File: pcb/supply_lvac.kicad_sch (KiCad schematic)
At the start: 46 parts

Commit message: Start layout
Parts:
- added H1, H2, H3, H4: MountingHole, MountingHole:MountingHole_3.2mm_M3, symbol Mechanical:MountingHole
- C1, C2, C3, C4, C5, C6: renamed from C?; footprint (none) -> Capacitor_THT:CP_Radial_D16.0mm_P7.50mm
- C10: renamed from C?; footprint (none) -> Capacitor_THT:CP_Radial_D4.0mm_P1.50mm
- C11, C12, C13, C14, C15, C16, C17, C18, C19, C20, C21, C22, C23, C24, C25, C26, C8: renamed from C?; footprint (none) -> Capacitor_THT:CP_Radial_D4.0mm_P2.00mm
- C7, C9: renamed from C?; footprint (none) -> Capacitor_THT:C_Disc_D3.0mm_W1.6mm_P2.50mm
- D6, D7: renamed from D?; footprint (none) -> LED_THT:LED_D5.0mm
- J1: renamed from J?; footprint (none) -> Connector_Molex:Molex_KK-254_AE-6410-02A_1x02_P2.54mm_Vertical
- J2, J3, J4, J5, J6, J7, J8, J9: renamed from J?; footprint (none) -> Connector_IDC:IDC-Header_2x05_P2.54mm_Vertical
- R1, R2: renamed from R?; footprint (none) -> Resistor_THT:R_Axial_DIN0207_L6.3mm_D2.5mm_P10.16mm_Horizontal
- U1, U2: renamed from U?; footprint (none) -> Package_TO_SOT_THT:TO-220-3_Vertical
- gave numbers to parts that had none: 5
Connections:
- net GND: now also C2.2, C5.1; no longer C2.1, C5.2
- net VREC+: now also C2.1; no longer C5.1
- net VREC-: now also C5.2; no longer C2.2
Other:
- moved on the sheet: C1, C10, C11, C12, C13, C14, C15, C16, C17, C18, C19, C2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

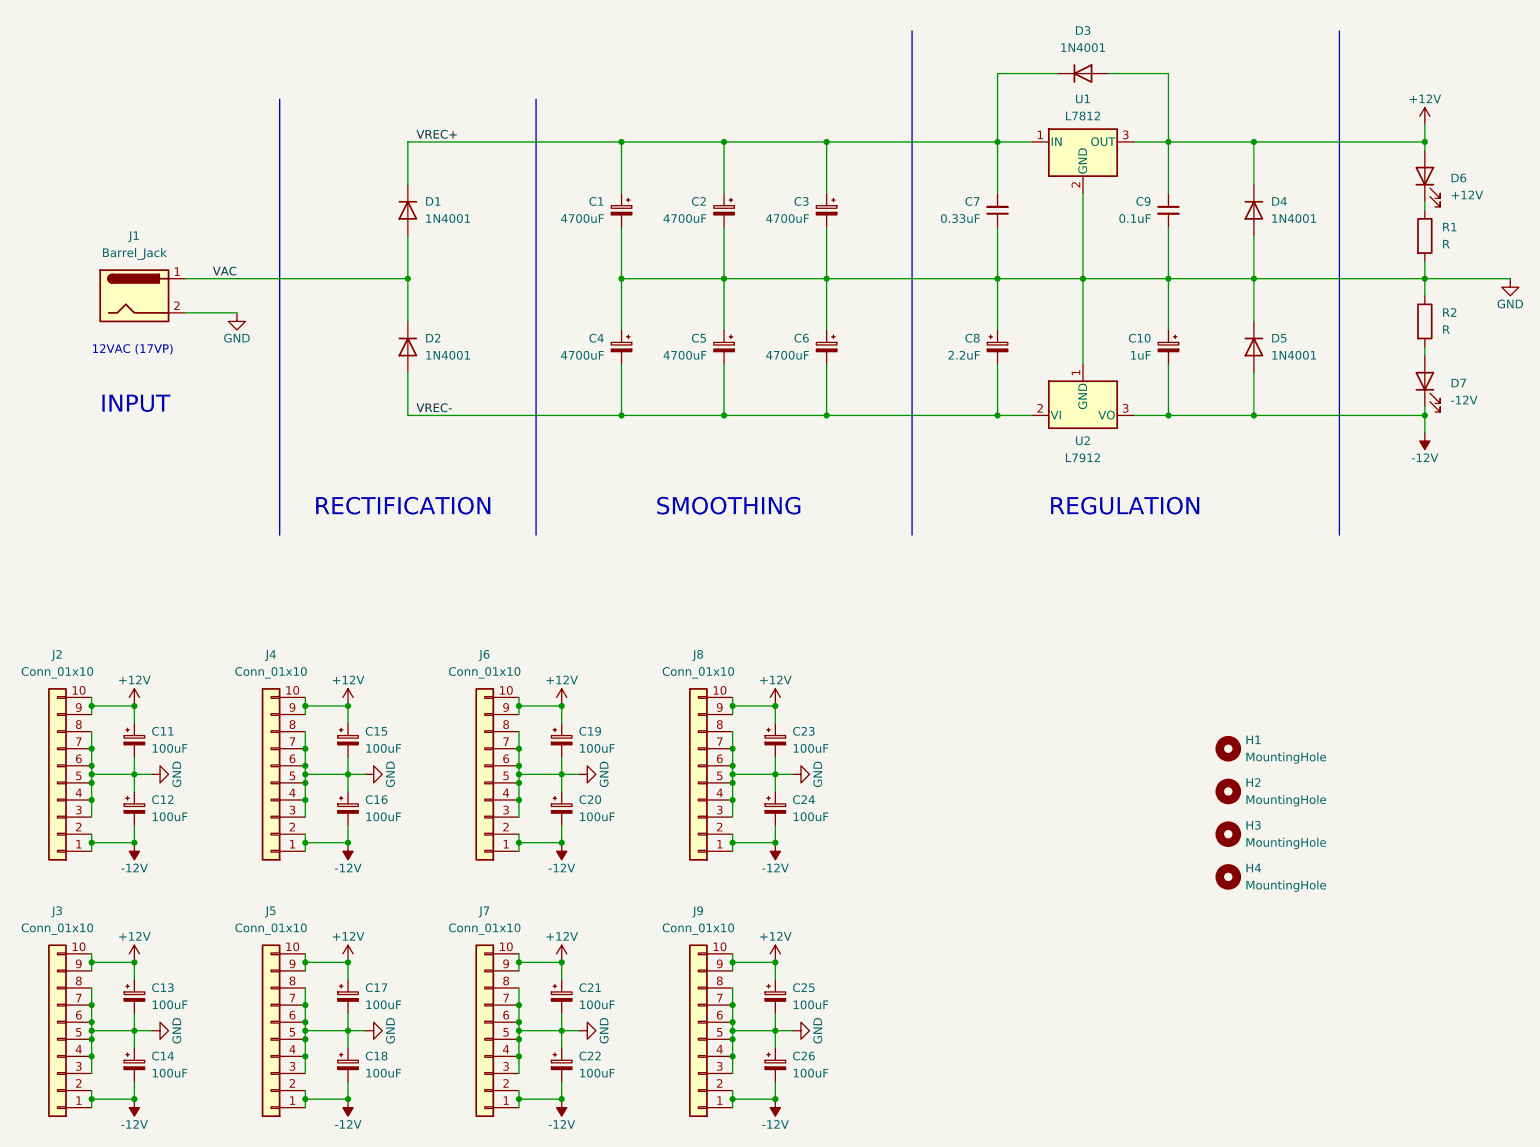
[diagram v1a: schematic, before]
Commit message: Start via stitching
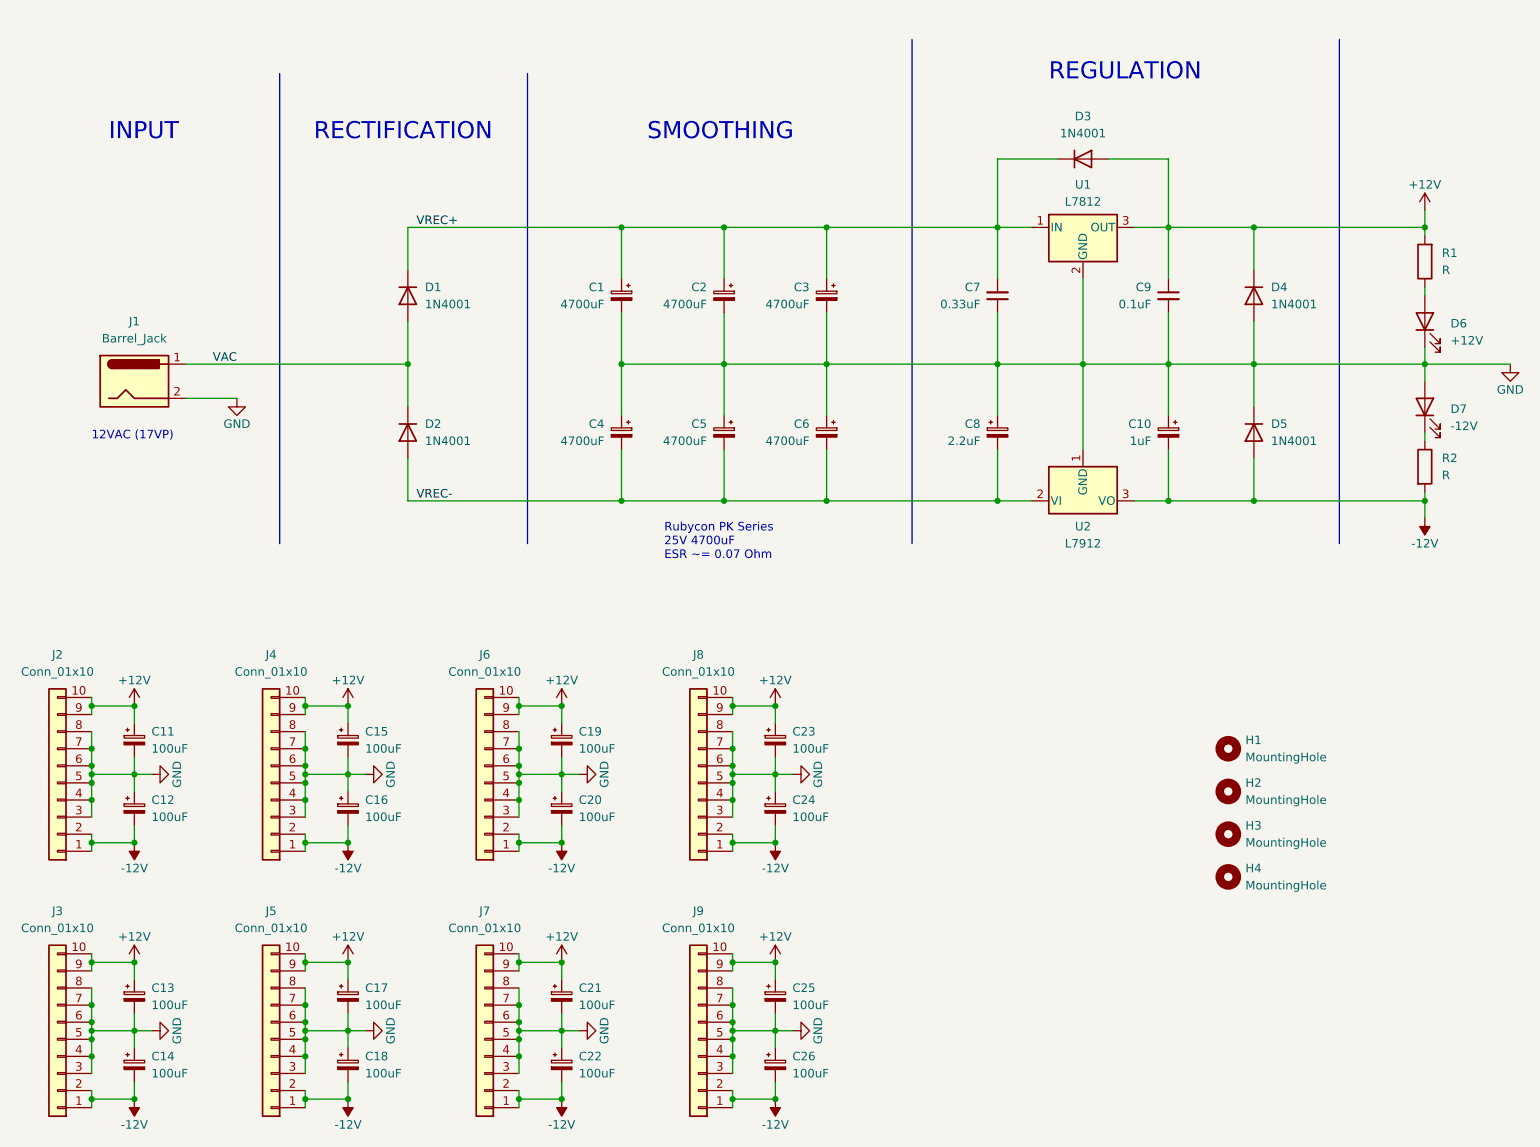
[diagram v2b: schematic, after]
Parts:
- R1, R2: footprint Resistor_THT:R_Axial_DIN0207_L6.3mm_D2.5mm_P10.16mm_Horizontal -> Resistor_THT:R_Axial_DIN0207_L6.3mm_D2.5mm_P2.54mm_Vertical
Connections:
- net +12V: now also R1.2; no longer D6.2 (A)
- net -12V: now also R2.2; no longer D7.1 (K)
- net GND: now also D6.1 (K), D7.2 (A); no longer R1.2, R2.1
- net at R1.1: now also D6.2 (A); no longer D6.1 (K)
- new net: D7.1 (K), R2.1
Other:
- note added: "Rubycon PK Series 25V 4700uF ESR ~= 0.07 Ohm"
- moved on the sheet: C1, C10, C2, C3, C4, C5, C6, C7, C8, C9, D1, D2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

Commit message: Complete layout. Export gerbers
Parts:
- removed C25, C26: 100uF, Capacitor_THT:CP_Radial_D4.0mm_P2.00mm, symbol Device:C_Polarized_Small
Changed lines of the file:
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@@
   (junction (at 132.08 125.73) (diameter 0) (color 0 0 0 0)
   )
-  (junction (at 138.43 173.99) (diameter 0) (color 0 0 0 0)
-  )
   (junction (at 43.18 173.99) (diameter 0) (color 0 0 0 0)
   )
@@
   (junction (at 209.55 74.93) (diameter 0) (color 0 0 0 0)
   )
-  (junction (at 138.43 184.15) (diameter 0) (color 0 0 0 0)
-  )
   (junction (at 74.93 163.83) (diameter 0) (color 0 0 0 0)
   )
-  (junction (at 138.43 163.83) (diameter 0) (color 0 0 0 0)
-  )
   (junction (at 43.18 135.89) (diameter 0) (color 0 0 0 0)
   )
@@
     (stroke (width 0) (type default) (color 0 0 0 0))
   )
-  (wire (pts (xy 138.43 181.61) (xy 138.43 184.15))
-    (stroke (width 0) (type default) (color 0 0 0 0))
-  )
   (wire (pts (xy 74.93 181.61) (xy 74.93 184.15))
     (stroke (width 0) (type default) (color 0 0 0 0))
@@
     (stroke (width 0) (type default) (color 0 0 0 0))
   )
+  (wire (pts (xy 68.58 172.72) (xy 68.58 173.99))
+    (stroke (width 0) (type default) (color 0 0 0 0))
+  )
+  (polyline (pts (xy 158.75 26.67) (xy 158.75 101.6))
+    (stroke (width 0) (type default) (color 0 0 0 0))
+  )
+  (wire (pts (xy 36.83 163.83) (xy 36.83 165.1))
+    (stroke (width 0) (type default) (color 0 0 0 0))
+  )
+  (wire (pts (xy 100.33 162.56) (xy 100.33 163.83))
+    (stroke (width 0) (type default) (color 0 0 0 0))
+  )
+  (wire (pts (xy 83.82 88.9) (xy 83.82 95.25))
+    (stroke (width 0) (type default) (color 0 0 0 0))
+  )
+  (wire (pts (xy 74.93 143.51) (xy 74.93 146.05))
+    (stroke (width 0) (type default) (color 0 0 0 0))
+  )
+  (wire (pts (xy 209.55 68.58) (xy 209.55 74.93))
+    (stroke (width 0) (type default) (color 0 0 0 0))
+  )
+  (wire (pts (xy 36.83 184.15) (xy 36.83 185.42))
+    (stroke (width 0) (type default) (color 0 0 0 0))
+  )
+  (wire (pts (xy 138.43 135.89) (xy 138.43 138.43))
+    (stroke (width 0) (type default) (color 0 0 0 0))
+  )
+  (wire (pts (xy 100.33 139.7) (xy 100.33 142.24))
+    (stroke (width 0) (type default) (color 0 0 0 0))
+  )
+  (wire (pts (xy 36.83 124.46) (xy 36.83 125.73))
+    (stroke (width 0) (type default) (color 0 0 0 0))
+  )
+  (wire (pts (xy 68.58 177.8) (xy 68.58 180.34))
+    (stroke (width 0) (type default) (color 0 0 0 0))
+  )
+  (wire (pts (xy 115.57 74.93) (xy 130.81 74.93))
+    (stroke (width 0) (type default) (color 0 0 0 0))
+  )
+  (wire (pts (xy 36.83 175.26) (xy 36.83 177.8))
+    (stroke (width 0) (type default) (color 0 0 0 0))
+  )
+  (wire (pts (xy 106.68 171.45) (xy 106.68 173.99))
+    (stroke (width 0) (type default) (color 0 0 0 0))
+  )
   (wire (pts (xy 132.08 173.99) (xy 138.43 173.99))
     (stroke (width 0) (type default) (color 0 0 0 0))
   )
-  (wire (pts (xy 68.58 172.72) (xy 68.58 173.99))
-    (stroke (width 0) (type default) (color 0 0 0 0))
-  )
-  (polyline (pts (xy 158.75 26.67) (xy 158.75 101.6))
-    (stroke (width 0) (type default) (color 0 0 0 0))
-  )
-  (wire (pts (xy 36.83 163.83) (xy 36.83 165.1))
-    (stroke (width 0) (type default) (color 0 0 0 0))
-  )
-  (wire (pts (xy 100.33 162.56) (xy 100.33 163.83))
-    (stroke (width 0) (type default) (color 0 0 0 0))
-  )
-  (wire (pts (xy 138.43 173.99) (xy 138.43 176.53))
-    (stroke (width 0) (type default) (color 0 0 0 0))
-  )
-  (wire (pts (xy 83.82 88.9) (xy 83.82 95.25))
-    (stroke (width 0) (type default) (color 0 0 0 0))
-  )
-  (wire (pts (xy 74.93 143.51) (xy 74.93 146.05))
-    (stroke (width 0) (type default) (color 0 0 0 0))
-  )
-  (wire (pts (xy 209.55 68.58) (xy 209.55 74.93))
-    (stroke (width 0) (type default) (color 0 0 0 0))
-  )
-  (wire (pts (xy 36.83 184.15) (xy 36.83 185.42))
-    (stroke (width 0) (type default) (color 0 0 0 0))
-  )
-  (wire (pts (xy 138.43 135.89) (xy 138.43 138.43))
-    (stroke (width 0) (type default) (color 0 0 0 0))
-  )
-  (wire (pts (xy 100.33 139.7) (xy 100.33 142.24))
-    (stroke (width 0) (type default) (color 0 0 0 0))
-  )
-  (wire (pts (xy 36.83 124.46) (xy 36.83 125.73))
-    (stroke (width 0) (type default) (color 0 0 0 0))
-  )
-  (wire (pts (xy 68.58 177.8) (xy 68.58 180.34))
-    (stroke (width 0) (type default) (color 0 0 0 0))
-  )
-  (wire (pts (xy 115.57 74.93) (xy 130.81 74.93))
-    (stroke (width 0) (type default) (color 0 0 0 0))
-  )
-  (wire (pts (xy 36.83 175.26) (xy 36.83 177.8))
-    (stroke (width 0) (type default) (color 0 0 0 0))
-  )
-  (wire (pts (xy 106.68 171.45) (xy 106.68 173.99))
-    (stroke (width 0) (type default) (color 0 0 0 0))
-  )
-  (wire (pts (xy 138.43 173.99) (xy 140.97 173.99))
-    (stroke (width 0) (type default) (color 0 0 0 0))
-  )
   (wire (pts (xy 36.83 177.8) (xy 36.83 180.34))
     (stroke (width 0) (type default) (color 0 0 0 0))
@@
     (stroke (width 0) (type default) (color 0 0 0 0))
   )
-  (wire (pts (xy 138.43 171.45) (xy 138.43 173.99))
-    (stroke (width 0) (type default) (color 0 0 0 0))
-  )
   (wire (pts (xy 130.81 82.55) (xy 130.81 74.93))
     (stroke (width 0) (type default) (color 0 0 0 0))
@@
   )
   (wire (pts (xy 43.18 163.83) (xy 43.18 166.37))
-    (stroke (width 0) (type default) (color 0 0 0 0))
-  )
-  (wire (pts (xy 138.43 163.83) (xy 138.43 166.37))
     (stroke (width 0) (type default) (color 0 0 0 0))
   )
@@
     )
   )
-  (symbol (lib_id "power:GND") (at 140.97 173.99 90) (unit 1)
-    (in_bom yes) (on_board yes)
-    (property "Reference" "#PWR028" (id 0) (at 147.32 173.99 0)
-      (effects (font (size 1.27 1.27)) hide)
-    )
-    (property "Value" "GND" (id 1) (at 144.78 173.99 0))
-    (property "Footprint" "" (id 2) (at 140.97 173.99 0)
-      (effects (font (size 1.27 1.27)) hide)
-    )
-    (property "Datasheet" "" (id 3) (at 140.97 173.99 0)
+  (symbol (lib_id "power:GND") (at 138.43 173.99 0) (unit 1)
+    (in_bom yes) (on_board yes)
+    (property "Reference" "#PWR028" (id 0) (at 138.43 180.34 0)
+      (effects (font (size 1.27 1.27)) hide)
+    )
+    (property "Value" "GND" (id 1) (at 138.43 177.8 0))
+    (property "Footprint" "" (id 2) (at 138.43 173.99 0)
+      (effects (font (size 1.27 1.27)) hide)
+    )
+    (property "Datasheet" "" (id 3) (at 138.43 173.99 0)
       (effects (font (size 1.27 1.27)) hide)
     )
@@
     (pin "1")
   )
-  (symbol (lib_id "Device:C_Polarized_Small") (at 138.43 168.91 0) (unit 1)
-    (in_bom yes) (on_board yes)
-    (property "Reference" "C25" (id 0) (at 140.97 167.64 0)
-      (effects (font (size 1.27 1.27)) (justify left))
-    )
-    (property "Value" "100uF" (id 1) (at 140.97 170.18 0)
-      (effects (font (size 1.27 1.27)) (justify left))
-    )
-    (property "Footprint" "Capacitor_THT:CP_Radial_D4.0mm_P2.00mm" (id 2) (at 138.43 168.91 0)
-      (effects (font (size 1.27 1.27)) hide)
-    )
-    (property "Datasheet" "~" (id 3) (at 138.43 168.91 0)
-      (effects (font (size 1.27 1.27)) hide)
-    )
-    (pin "1")
-    (pin "2")
-  )
   (symbol (lib_id "Connector_Generic:Conn_01x10") (at 127 175.26 180) (unit 1)
     (in_bom yes) (on_board yes) (fields_autoplaced)
@@
     (pin "2")
   )
-  (symbol (lib_id "Device:C_Polarized_Small") (at 138.43 179.07 0) (unit 1)
-    (in_bom yes) (on_board yes)
-    (property "Reference" "C26" (id 0) (at 140.97 177.8 0)
-      (effects (font (size 1.27 1.27)) (justify left))
-    )
-    (property "Value" "100uF" (id 1) (at 140.97 180.34 0)
-      (effects (font (size 1.27 1.27)) (justify left))
-    )
-    (property "Footprint" "Capacitor_THT:CP_Radial_D4.0mm_P2.00mm" (id 2) (at 138.43 179.07 0)
-      (effects (font (size 1.27 1.27)) hide)
-    )
-    (property "Datasheet" "~" (id 3) (at 138.43 179.07 0)
-      (effects (font (size 1.27 1.27)) hide)
-    )
-    (pin "1")
-    (pin "2")
-  )
   (symbol (lib_id "power:-12V") (at 74.93 146.05 180) (unit 1)
     (in_bom yes) (on_board yes)
@@
       (reference "C24") (unit 1) (value "100uF") (footprint "Capacitor_THT:CP_Radial_D4.0mm_P2.00mm")
     )
-    (path "/8942a937-6aba-46b1-9710-b39095d859c1"
-      (reference "C25") (unit 1) (value "100uF") (footprint "Capacitor_THT:CP_Radial_D4.0mm_P2.00mm")
-    )
-    (path "/b72efed7-6066-4a80-ad6f-da3877f964dd"
-      (reference "C26") (unit 1) (value "100uF") (footprint "Capacitor_THT:CP_Radial_D4.0mm_P2.00mm")
-    )
     (path "/a456bd40-b2fd-424c-b931-b7b320bd8eee"
